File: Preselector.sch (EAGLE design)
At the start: 134 parts, among them IC58 LMZ31707RVQ, Q2 FDV303N, X1 0733660061, X2 0733660061, X3 0733660061, X4 0733660061, X5 0733660061, X6 0733660061, X7 0733660061, X8 0733660061

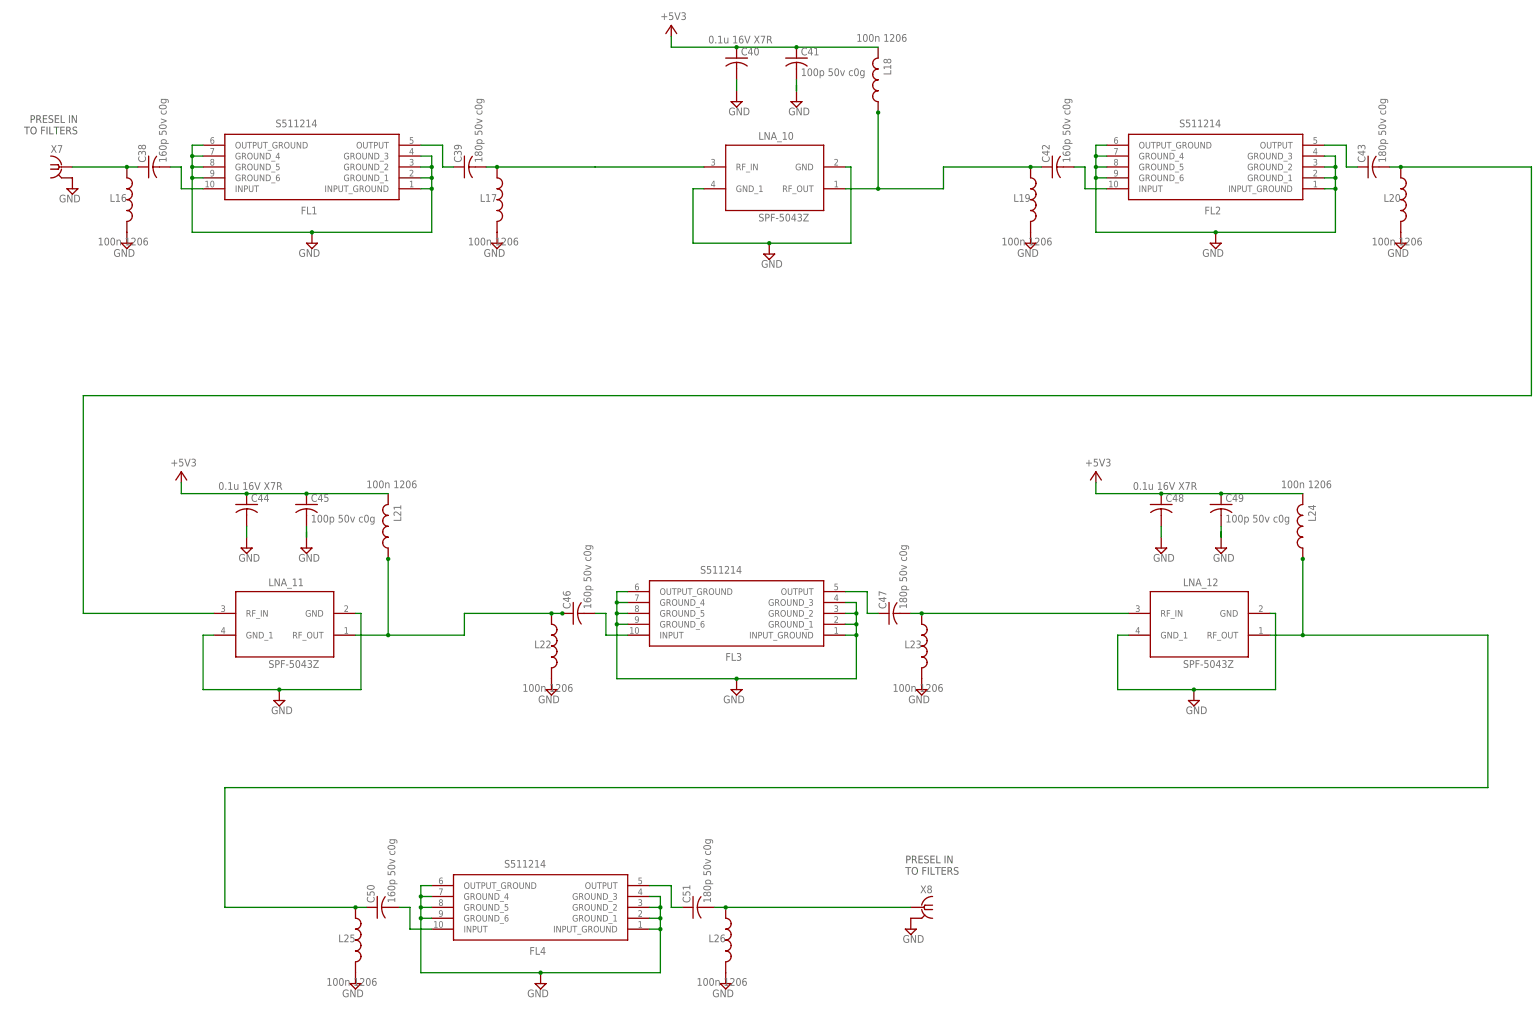
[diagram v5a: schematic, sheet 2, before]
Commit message: Renamed 4m net, look at the naming convention on there to continue. I also renamed the beginning of the 2m band, I'm renaming the 5v3 net to just +5v. I think the voltage can be the same name because it will connect to a power plane.
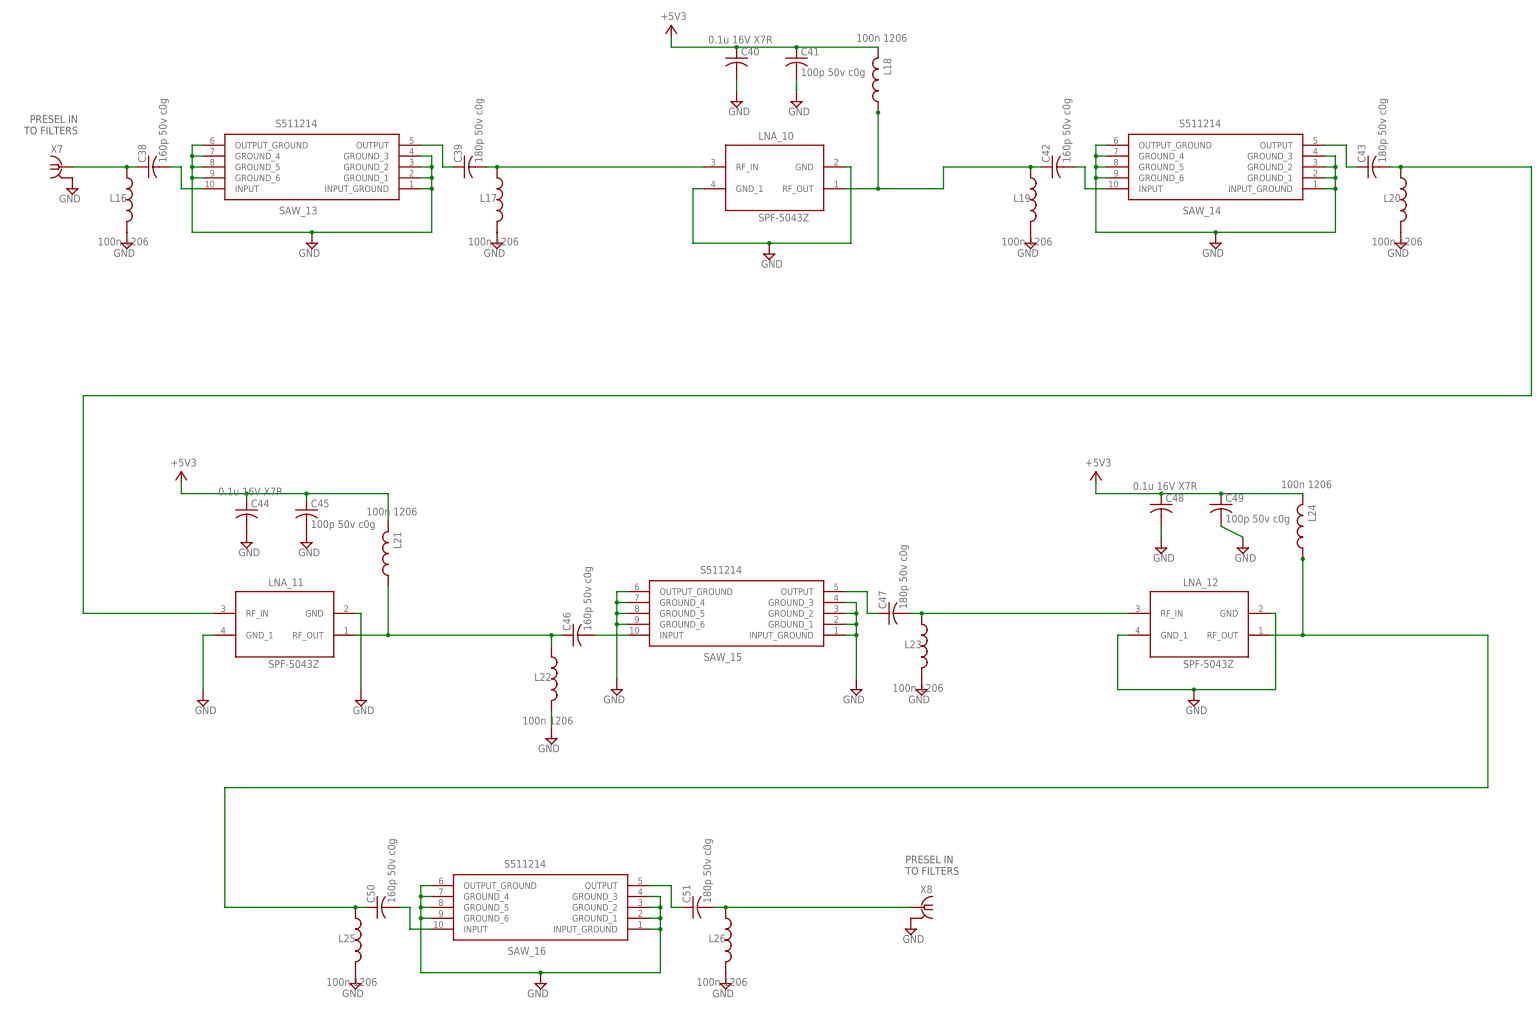
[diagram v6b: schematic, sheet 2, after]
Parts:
- renumbered FL1 to SAW_13, FL2 to SAW_14, FL3 to SAW_15, FL4 to SAW_16
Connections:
- net 4M_RF_IN1 renamed SAW_14_OUT
- removed net GND3: L12.1
- removed net N$2: C13.2, X2G$1.1
- new net +5V: C40.1, C41.1, C44.1, C45.1, L18.2, L21.2
- new net 2M_RF_IN_14: C1.2, LNA_1.RF_IN
- new net 2M_RF_IN_2: C4.1, L1.1, LNA_1.RF_OUT
- new net 2M_RF_IN_3: C4.2, L2.2, SAW_2.INPUT
- new net 2M_RF_IN_4: C5.1, L3.2, SAW_2.OUTPUT
- new net 2M_RF_IN_5: C5.2, LNA_2.RF_IN
- new net 2M_RF_IN_6: C8.1, L4.1, LNA_2.RF_OUT
- new net 2M_RF_IN_7: C8.2, L5.2, SAW_3.INPUT
- new net 2M_RF_IN_9: C9.1, L6.2, SAW_3.OUTPUT
- new net 4M_RF_OUT: C51.2, L26.1, X8G$1.1
- new net LNA_10_IN: C39.2, L17.1, LNA_10.RF_IN
- new net LNA_10_OUT: C42.1, L18.1, L19.1, LNA_10.RF_OUT
- new net LNA_11_IN: C43.2, L20.1, LNA_11.RF_IN
- new net LNA_11_OUT: C46.1, L21.1, L22.1, LNA_11.RF_OUT
- new net LNA_12_IN: C47.2, L23.1, LNA_12.RF_IN
- new net LNA_12_OUT: C50.1, L24.1, L25.1, LNA_12.RF_OUT
- new net LNA_3_IN: C12.1, L7.2, LNA_3.RF_OUT
- new net LNA_3_OUT: C9.2, LNA_3.RF_IN
- new net SAW_13_IN: C38.2, SAW_13.INPUT
- new net SAW_13_OUT: C39.1, SAW_13.OUTPUT
- new net SAW_14_IN: C42.2, SAW_14.INPUT
- new net SAW_15_IN: C46.2, SAW_15.INPUT
- new net SAW_15_OUT: C47.1, SAW_15.OUTPUT
- new net SAW_16_IN: C50.2, SAW_16.INPUT
- new net SAW_16_OUT: C51.1, SAW_16.OUTPUT
- new net SAW_1_OUT: C1.1, SAW_1.OUTPUT
- new net SAW_4_IN: C13.1, L9.2, SAW_4.OUTPUT
- new net SAW_4_OUT: C12.2, L8.2, SAW_4.INPUT
- net +5V3: no longer C40.1, C41.1, C44.1, C45.1, L18.2, L21.2
- net 2M_RF_IN: now also C13.2, X2G$1.1; no longer C1.1, C1.2, C12.1, C12.2, C13.1, C4.1, C4.2, C5.1, C5.2, C8.1, C8.2, C9.1, C9.2, L1.1, L2.2, L3.2, L4.1, L5.2, L6.2, L7.2, L8.2, L9.2, LNA_1.RF_IN, LNA_1.RF_OUT, LNA_2.RF_IN, LNA_2.RF_OUT, LNA_3.RF_IN, LNA_3.RF_OUT, SAW_1.OUTPUT, SAW_2.INPUT, SAW_2.OUTPUT, SAW_3.INPUT, SAW_3.OUTPUT, SAW_4.INPUT, SAW_4.OUTPUT
- net 4M_RF_IN: no longer C38.2, C39.1, C39.2, C42.1, C42.2, C43.2, C46.1, C46.2, C47.1, C47.2, C50.1, C50.2, C51.1, C51.2, L17.1, L18.1, L19.1, L20.1, L21.1, L22.1, L23.1, L24.1, L25.1, L26.1, LNA_10.RF_IN, LNA_10.RF_OUT, LNA_11.RF_IN, LNA_11.RF_OUT, LNA_12.RF_IN, LNA_12.RF_OUT, SAW_13.INPUT, SAW_13.OUTPUT, SAW_14.INPUT, SAW_15.INPUT, SAW_15.OUTPUT, SAW_16.INPUT, SAW_16.OUTPUT, X8G$1.1
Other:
- moved on the sheet: C44, C45, C46, L21, L22
